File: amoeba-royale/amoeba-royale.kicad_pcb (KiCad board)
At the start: 2 copper layers, 18.8 x 18.1 mm, 48 parts

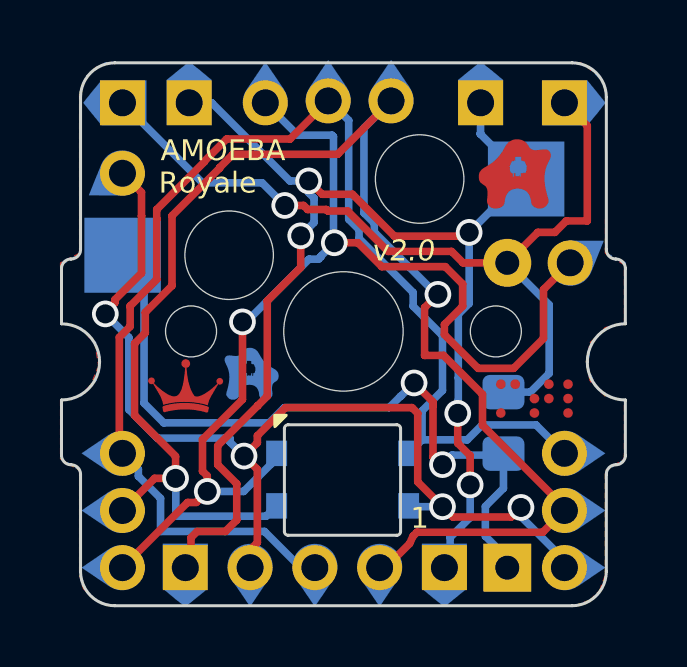
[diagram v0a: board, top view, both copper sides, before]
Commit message: Create a JSON file with KiKit option for panelization
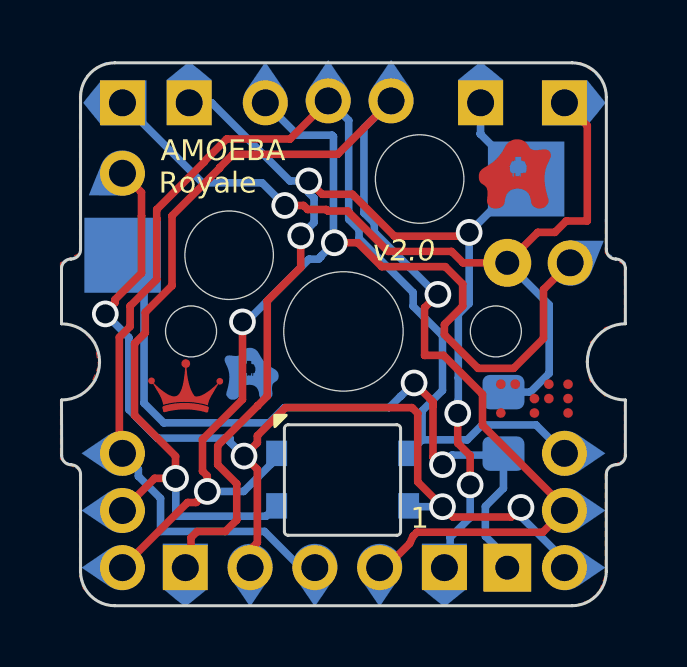
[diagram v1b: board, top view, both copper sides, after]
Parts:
- added REF**: Tab, kikit:Tab, B.Cu at (239.3, 113.8)
- added REF**: Tab, kikit:Tab, B.Cu at (239.3, 109.2)
- added REF**: Tab, kikit:Tab, B.Cu at (258.6, 113.8)
- added REF**: Tab, kikit:Tab, B.Cu at (258.6, 109.2)
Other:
- outline, holes or cut-outs redrawn
